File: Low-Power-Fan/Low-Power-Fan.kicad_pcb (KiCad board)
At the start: 2 copper layers, 10.5 x 16.4 mm, 9 parts, among them J1 in, J2 out, U1 FAN5333A

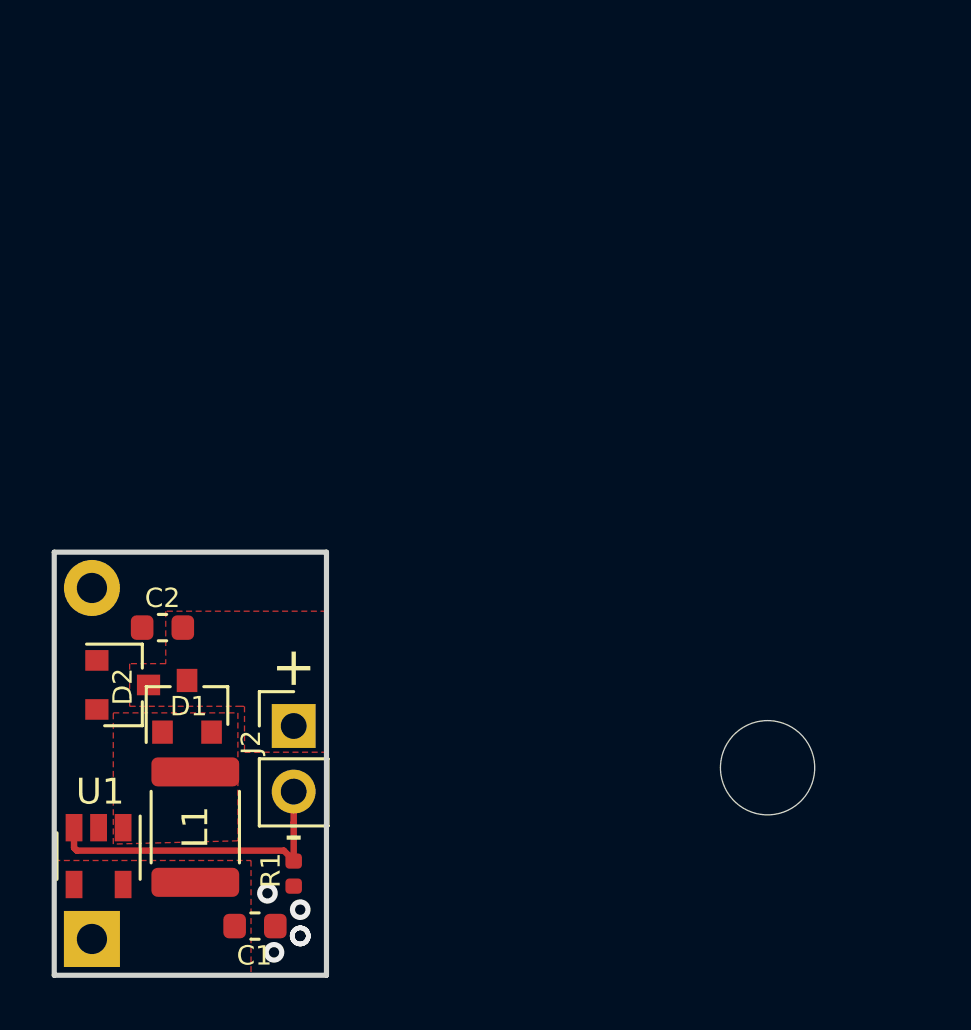
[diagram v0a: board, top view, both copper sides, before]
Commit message: Added 10 minute timer and a switch. Updated resistor for higher current.
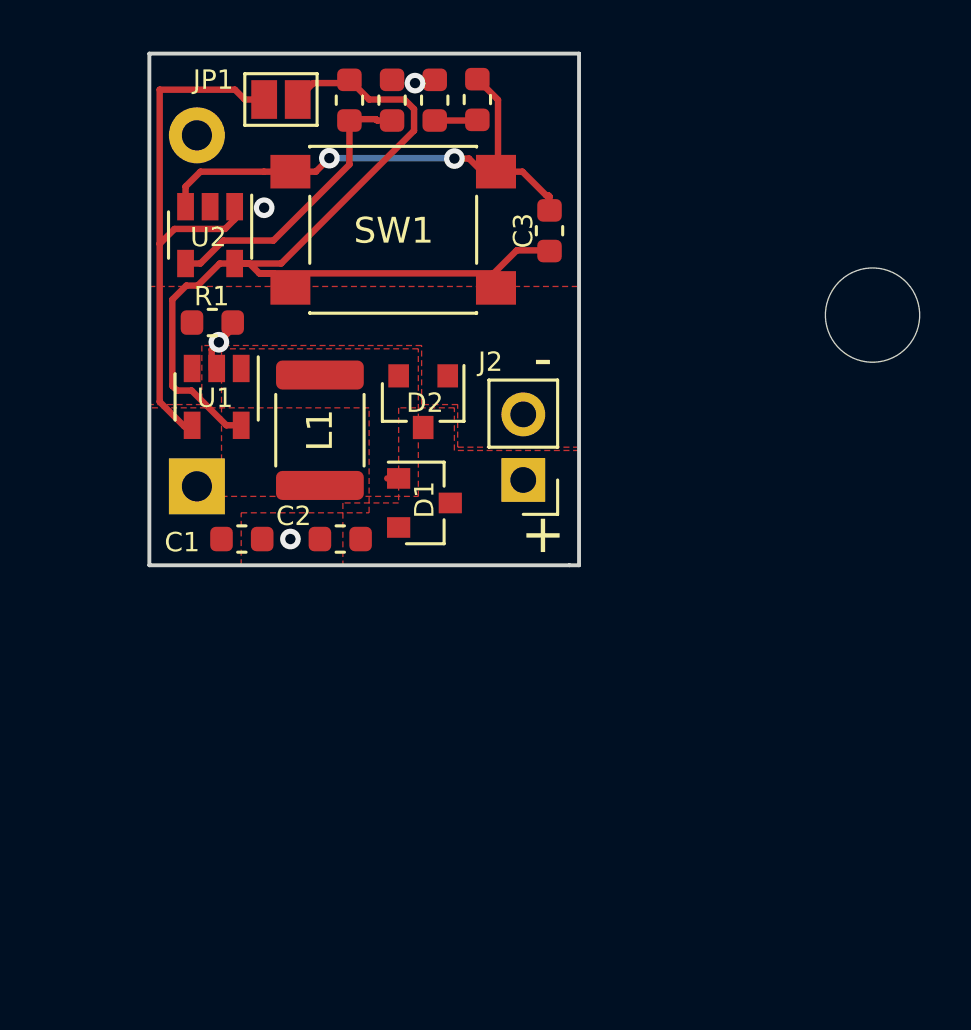
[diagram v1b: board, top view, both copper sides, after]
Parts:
- added C3: 22uF, Capacitor_SMD:C_0603_1608Metric, F.Cu at (129.3, 81.2)
- added JP1: jumper, Jumper:SolderJumper-2_P1.3mm_Open_Pad1.0x1.5mm, F.Cu at (118.9, 76.1)
- added R2: 22M, Resistor_SMD:R_0603_1608Metric, F.Cu at (121.5, 76.1)
- added R3: 22M, Resistor_SMD:R_0603_1608Metric, F.Cu at (123.2, 76.1)
- added R4: 22M, Resistor_SMD:R_0603_1608Metric, F.Cu at (126.5, 76.1)
- added R5: 22M, Resistor_SMD:R_0603_1608Metric, F.Cu at (124.8, 76.1)
- added REF**: OSHW-Logo_5.7x6mm_SilkScreen, Symbol:OSHW-Logo_5.7x6mm_SilkScreen, B.Cu at (121.1, 86.7)
- added SW1: SW_Push, Button_Switch_SMD:SW_SPST_PTS645, F.Cu at (123.2, 81.1)
- added U2: MCP6541, Package_TO_SOT_SMD:SOT-23-5, F.Cu at (116.1, 81.3)
- R1: value 10 -> 8.2; footprint Resistor_SMD:R_0402_1005Metric -> Resistor_SMD:R_0603_1608Metric
- moved R1 21.6 mm to (116.2, 84.7), turned to 0 degrees
- moved U1 18.4 mm to (116.4, 87.6)
- moved J1 18.0 mm to (115.6, 91.1)
- moved L1 16.1 mm to (120.4, 88.9)
- moved D2 16.0 mm to (124.4, 87.8), turned to 270 degrees
- moved C1 15.0 mm to (117.4, 93.1)
- moved J2 13.0 mm to (128.3, 90.8), turned to 180 degrees
- moved D1 12.1 mm to (124.4, 91.7), turned to 0 degrees
- moved C2 7.69 mm to (121.2, 93.1)
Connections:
- D2 pad 2: GND -> Net-(D2-Pad2)
- J2 pad 2: Net-(J2-Pad2) -> Net-(D2-Pad2)
- R1 pad 1: Net-(J2-Pad2) -> Net-(D2-Pad2)
- U1 pad 3: Net-(J2-Pad2) -> Net-(D2-Pad2)
- U1 pad 4: Net-(C1-Pad1) -> Net-(JP1-Pad2)
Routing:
- net Net-(C1-Pad1): track 0.00 -> 38.0 mm
- net Net-(JP1-Pad2): track 0.00 -> 22.1 mm
- net Net-(C3-Pad2): track 0.00 -> 20.2 mm, vias 0 -> 2
- net Net-(J2-Pad2): track 12.1 -> 0.00 mm
- net Net-(R2-Pad2): track 0.00 -> 11.2 mm
- net GND: track 0.00 -> 2.26 mm, vias 6 -> 4
- net Net-(R4-Pad2): track 0.00 -> 1.67 mm
- added copper zone on F.Cu, net Net-(D2-Pad2)
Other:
- board size 10.5 x 16.4 mm -> 16.6 x 19.8 mm
- net class Power removed
- board text added: "Low Power Fan Corwin Hansen"

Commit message: changed solder mask clearence to make reflow easier
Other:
- rule pad_to_mask_clearance: 0.051 -> 0
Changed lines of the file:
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@@
     (pad_size 1.524 1.524)
     (pad_drill 0.762)
-    (pad_to_mask_clearance 0.051)
+    (pad_to_mask_clearance 0)
     (solder_mask_min_width 0.25)
     (aux_axis_origin 0 0)

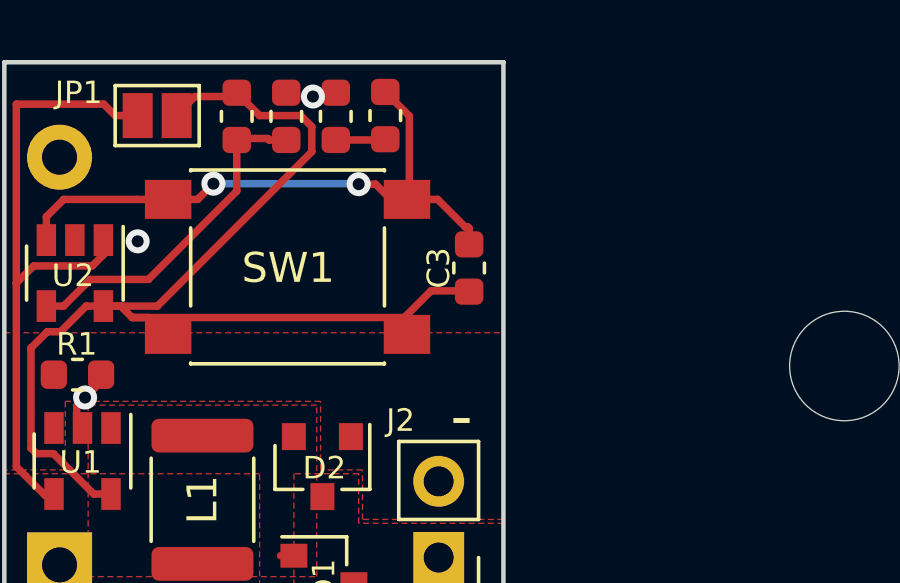
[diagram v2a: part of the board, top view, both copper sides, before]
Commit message: Capacitor 3 replaced with correct size
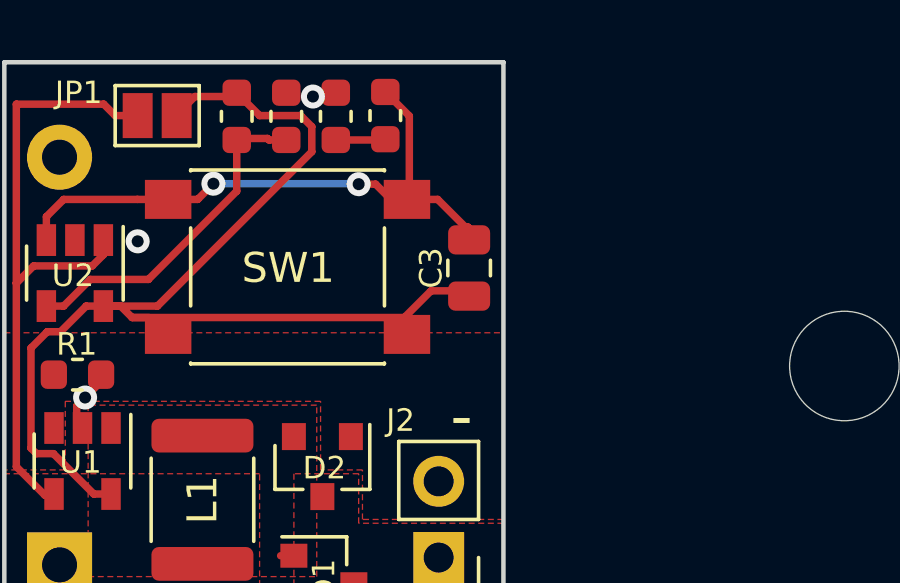
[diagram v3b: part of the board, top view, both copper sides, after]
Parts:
- removed REF**: OSHW-Logo_5.7x6mm_SilkScreen, Symbol:OSHW-Logo_5.7x6mm_SilkScreen
- C3: footprint Capacitor_SMD:C_0603_1608Metric -> Capacitor_SMD:C_0805_2012Metric

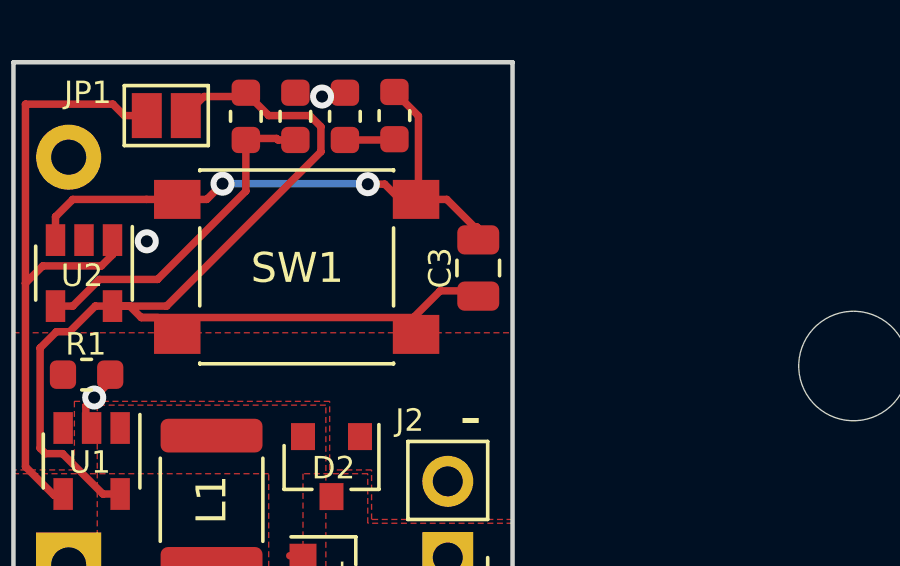
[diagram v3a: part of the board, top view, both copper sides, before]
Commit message: Connected one side of the capacitor to ground
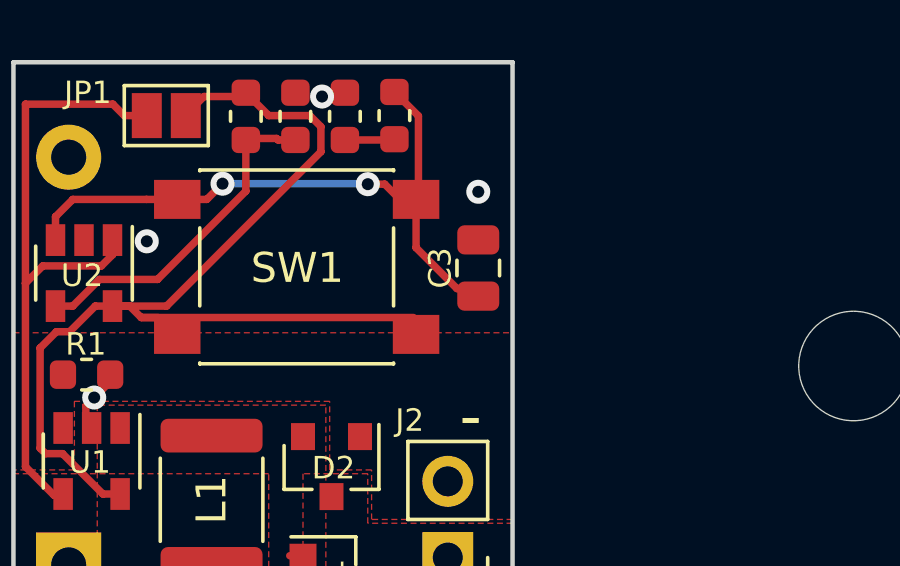
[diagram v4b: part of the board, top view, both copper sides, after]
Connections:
- C3 pad 1: Net-(C1-Pad1) -> Net-(C3-Pad1)
- C3 pad 2: Net-(C3-Pad2) -> GND
- R4 pad 1: Net-(C3-Pad2) -> Net-(C3-Pad1)
- SW1 pad 1: Net-(C3-Pad2) -> Net-(C3-Pad1)
- U2 pad 3: Net-(C3-Pad2) -> Net-(C3-Pad1)
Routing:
- net Net-(C3-Pad1): track 0.00 -> 21.4 mm, vias 0 -> 2
- net Net-(C3-Pad2): track 20.2 -> 0.00 mm, vias 2 -> 0
- net Net-(C1-Pad1): track 38.0 -> 35.5 mm
- net GND: vias 4 -> 5

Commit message: Revert "Connected one side of the capacitor to ground"
This reverts commit a7569e6a569e54939577e6c551374c5e72ad59fc.
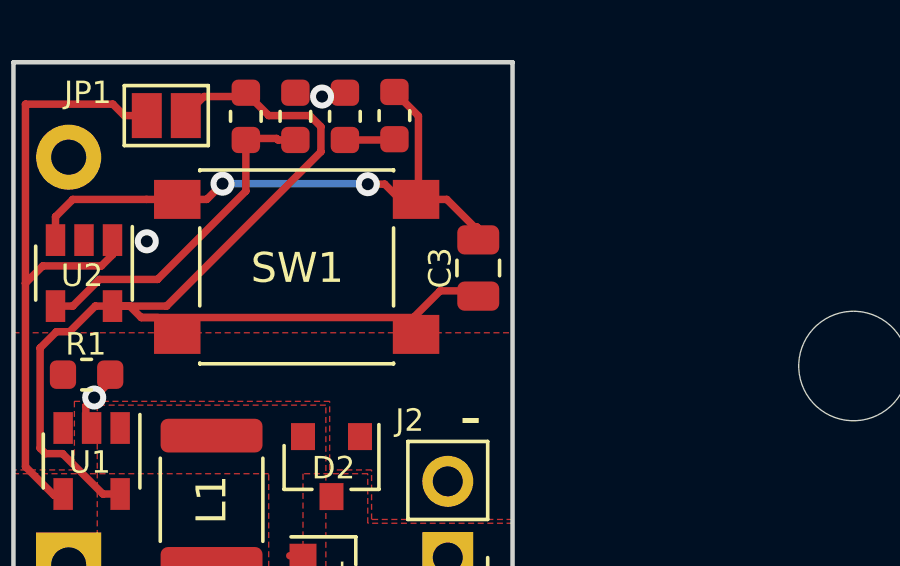
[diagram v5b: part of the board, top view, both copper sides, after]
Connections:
- C3 pad 1: Net-(C3-Pad1) -> Net-(C1-Pad1)
- C3 pad 2: GND -> Net-(C3-Pad2)
- R4 pad 1: Net-(C3-Pad1) -> Net-(C3-Pad2)
- SW1 pad 1: Net-(C3-Pad1) -> Net-(C3-Pad2)
- U2 pad 3: Net-(C3-Pad1) -> Net-(C3-Pad2)
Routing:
- net Net-(C3-Pad1): track 21.4 -> 0.00 mm, vias 2 -> 0
- net Net-(C3-Pad2): track 0.00 -> 20.2 mm, vias 0 -> 2
- net Net-(C1-Pad1): track 35.5 -> 38.0 mm
- net GND: vias 5 -> 4
